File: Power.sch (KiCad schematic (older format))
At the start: 24 parts, among them Q10 TT8M3TR, Q11 TT8M3TR, U2 NE555D, U3 LM337_TO263, U4 LM317LPW

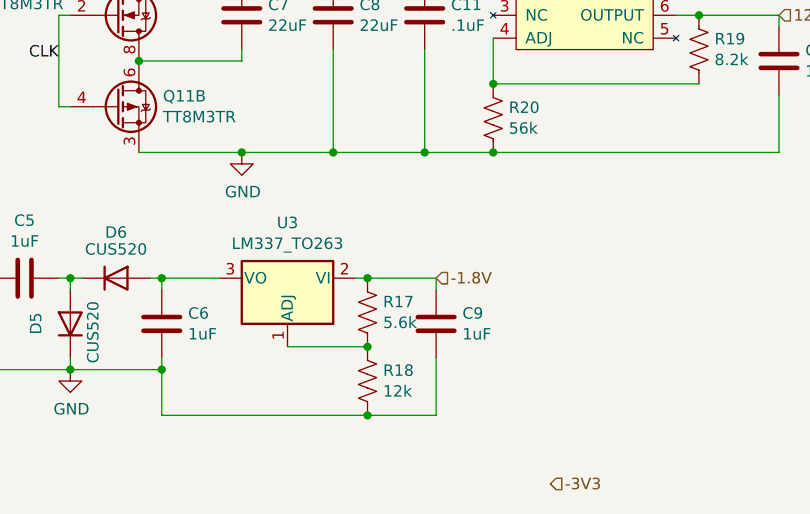
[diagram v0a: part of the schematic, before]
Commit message: Fixed symbol mismatch
The pins for the TLV274 symbol were incorrect.
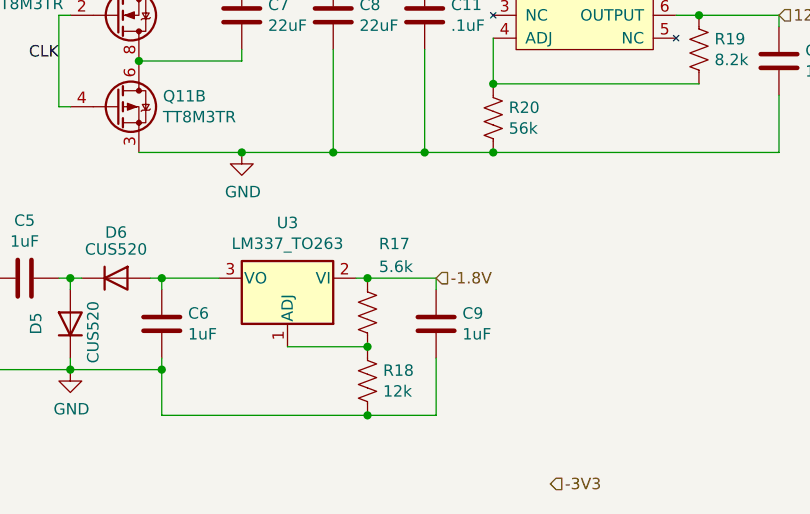
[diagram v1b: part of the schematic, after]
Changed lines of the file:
@@
 U 1 1 615210C6
 P 7400 3700
-F 0 "R17" H 7332 3654 50  0000 R CNN
-F 1 "5.6k" H 7332 3745 50  0000 R CNN
+F 0 "R17" H 7350 3400 50  0000 R CNN
+F 1 "5.6k" H 7350 3500 50  0000 R CNN
 F 2 "Resistor_SMD:R_0603_1608Metric_Pad0.98x0.95mm_HandSolder" V 7440 3690 50  0001 C CNN
 F 3 "~" H 7400 3700 50  0001 C CNN
